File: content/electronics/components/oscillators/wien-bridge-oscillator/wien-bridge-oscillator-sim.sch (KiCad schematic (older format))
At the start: 12 parts, among them U1 AD8051

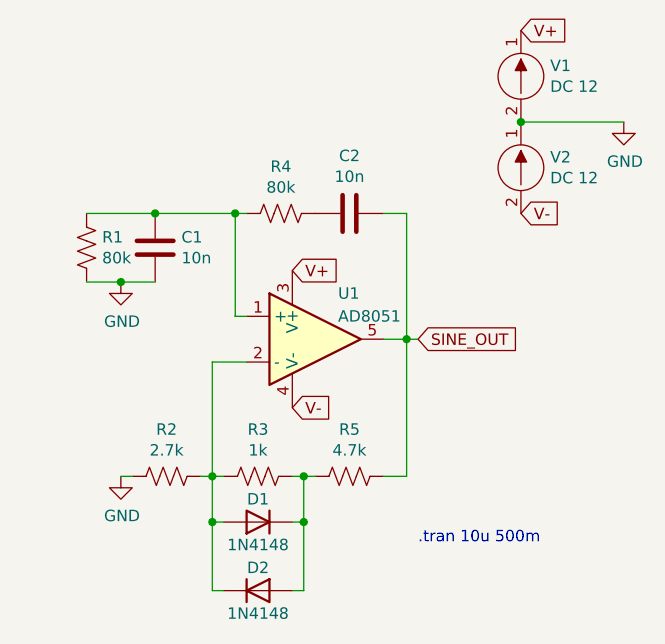
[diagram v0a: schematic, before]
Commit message: Added traditional schematics of a Wien bridge oscillator circuit.
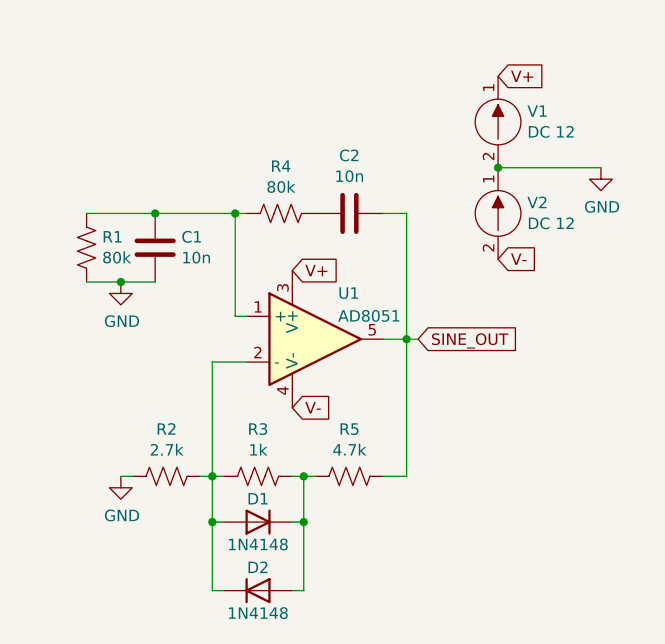
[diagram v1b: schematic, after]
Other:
- note removed: ".tran 10u 500m"
- moved on the sheet: V1, V2
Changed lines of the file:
@@
 L Bio-Sim:DC12 V1
 U 1 1 608A8BB9
-P 6200 1900
-F 0 "V1" H 6328 1946 50  0000 L CNN
-F 1 "DC 12" H 6328 1855 50  0000 L CNN
-F 2 "" H 6200 1900 50  0000 C CNN
-F 3 "" H 6200 1900 50  0000 C CNN
-F 4 "V" H 6450 1650 60  0001 C CNN "Spice_Primitive"
-F 5 "1 2" H 6450 1750 60  0001 C CNN "Spice_Node_Sequence"
-F 6 "ASK" H 6400 500 50  0001 C CNN "Substitution Category"
-	1    6200 1900
+P 6100 2100
+F 0 "V1" H 6228 2146 50  0000 L CNN
+F 1 "DC 12" H 6228 2055 50  0000 L CNN
+F 2 "" H 6100 2100 50  0000 C CNN
+F 3 "" H 6100 2100 50  0000 C CNN
+F 4 "V" H 6350 1850 60  0001 C CNN "Spice_Primitive"
+F 5 "1 2" H 6350 1950 60  0001 C CNN "Spice_Node_Sequence"
+F 6 "ASK" H 6300 700 50  0001 C CNN "Substitution Category"
+	1    6100 2100
 	1    0    0    -1
 $EndComp
@@
 L Bio-Sim:DC12 V2
 U 1 1 608A97CE
-P 6200 2300
-F 0 "V2" H 6328 2346 50  0000 L CNN
-F 1 "DC 12" H 6328 2255 50  0000 L CNN
-F 2 "" H 6200 2300 50  0000 C CNN
-F 3 "" H 6200 2300 50  0000 C CNN
-F 4 "V" H 6450 2050 60  0001 C CNN "Spice_Primitive"
-F 5 "1 2" H 6450 2150 60  0001 C CNN "Spice_Node_Sequence"
-F 6 "ASK" H 6400 900 50  0001 C CNN "Substitution Category"
-	1    6200 2300
+P 6100 2500
+F 0 "V2" H 6228 2546 50  0000 L CNN
+F 1 "DC 12" H 6228 2455 50  0000 L CNN
+F 2 "" H 6100 2500 50  0000 C CNN
+F 3 "" H 6100 2500 50  0000 C CNN
+F 4 "V" H 6350 2250 60  0001 C CNN "Spice_Primitive"
+F 5 "1 2" H 6350 2350 60  0001 C CNN "Spice_Node_Sequence"
+F 6 "ASK" H 6300 1100 50  0001 C CNN "Substitution Category"
+	1    6100 2500
 	1    0    0    -1
 $EndComp
@@
 L power:GND #PWR03
 U 1 1 608AA1F3
-P 6650 2100
-F 0 "#PWR03" H 6650 1850 50  0001 C CNN
-F 1 "GND" H 6655 1927 50  0000 C CNN
-F 2 "" H 6650 2100 50  0001 C CNN
-F 3 "" H 6650 2100 50  0001 C CNN
-	1    6650 2100
-	1    0    0    -1
-$EndComp
-Wire Wire Line
-	6650 2100 6200 2100
-Connection ~ 6200 2100
-Text GLabel 6200 2500 2    50   Input ~ 0
+P 6550 2300
+F 0 "#PWR03" H 6550 2050 50  0001 C CNN
+F 1 "GND" H 6555 2127 50  0000 C CNN
+F 2 "" H 6550 2300 50  0001 C CNN
+F 3 "" H 6550 2300 50  0001 C CNN
+	1    6550 2300
+	1    0    0    -1
+$EndComp
+Wire Wire Line
+	6550 2300 6100 2300
+Connection ~ 6100 2300
+Text GLabel 6100 2700 2    50   Input ~ 0
 V-
-Text GLabel 6200 1700 2    50   Input ~ 0
+Text GLabel 6100 1900 2    50   Input ~ 0
 V+
 Text GLabel 5200 2750 2    50   Input ~ 0
@@
 Wire Wire Line
 	4850 3150 5000 3150
-Text Notes 5750 3950 0    50   ~ 0
-.tran 10u 500m
 $EndSCHEMATC

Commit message: Updated the Wien bridge oscillator worked example.
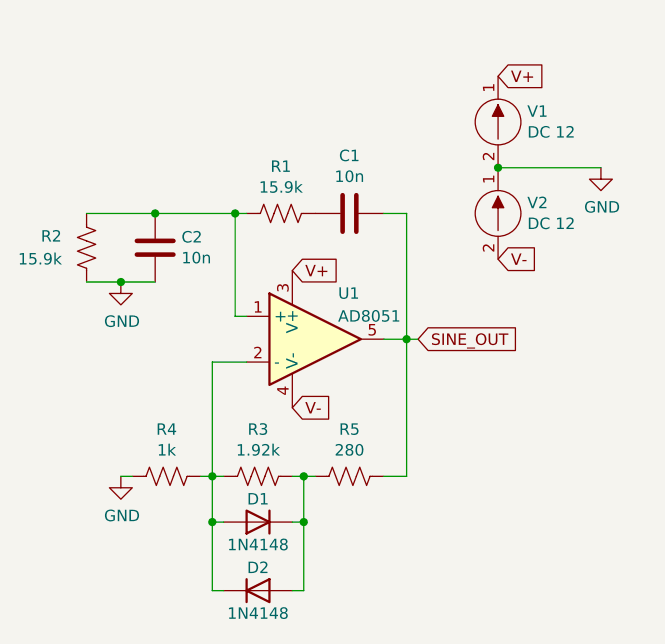
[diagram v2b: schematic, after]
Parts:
- D1, D2: Spice_Lib_File sim\\1N4148.lib -> 1N4148.lib
- R1: renamed from R4; value 80k -> 15.9k
- R2: renamed from R1; value 80k -> 15.9k
- R3: value 1k -> 1.92k
- R4: renamed from R2; value 2.7k -> 1k
- R5: value 4.7k -> 280
- U1: Spice_Lib_File sim\\AD8051.lib -> AD8051.lib
- renumbered C2 to C1, C1 to C2
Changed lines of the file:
@@
 $EndDescr
-$Comp
-L mbedded-ninja-kicad-symbols-sim:1N4148 D2
-U 1 1 608A7C60
-P 5050 4150
-F 0 "D2" H 5050 4250 50  0000 C CNN
-F 1 "1N4148" H 5050 4050 50  0000 C CNN
-F 2 "" H 5050 4150 50  0001 C CNN
-F 3 "~" H 5050 4150 50  0001 C CNN
-F 4 "D" H 5050 3650 50  0001 C CNN "Spice_Primitive"
-F 5 "1N4148" H 5050 3750 50  0001 C CNN "Spice_Model"
-F 6 "Y" H 5050 3850 50  0001 C CNN "Spice_Netlist_Enabled"
-F 7 "2 1" H 5050 3950 50  0001 C CNN "Spice_Node_Sequence"
-F 8 "sim\\1N4148.lib" H 5050 3550 50  0001 C CNN "Spice_Lib_File"
-	1    5050 4150
-	1    0    0    -1
-$EndComp
 $Comp
 L mbedded-ninja-kicad-symbols-sim:1N4148 D1
@@
 F 6 "Y" H 5050 3550 50  0001 C CNN "Spice_Netlist_Enabled"
 F 7 "2 1" H 5050 3650 50  0001 C CNN "Spice_Node_Sequence"
-F 8 "sim\\1N4148.lib" H 5050 3250 50  0001 C CNN "Spice_Lib_File"
+F 8 "1N4148.lib" H 5050 3250 50  0001 C CNN "Spice_Lib_File"
 	1    5050 3850
 	-1   0    0    1
@@
 F 5 "AD8051" H 5300 3300 50  0001 L CNN "Spice_Model"
 F 6 "Y" H 5300 3300 50  0001 L CNN "Spice_Netlist_Enabled"
-F 7 "sim\\AD8051.lib" H 5300 3300 50  0001 L CNN "Spice_Lib_File"
+F 7 "AD8051.lib" H 5300 3300 50  0001 L CNN "Spice_Lib_File"
 	1    5300 3050
 	1    0    0    -1
@@
 	5600 3050 5700 3050
 $Comp
-L mbedded-ninja-kicad-symbols-sim:10k R4
+L mbedded-ninja-kicad-symbols-sim:10k R1
 U 1 1 608B013F
 P 5150 2500
-F 0 "R4" V 4945 2500 50  0000 C CNN
-F 1 "80k" V 5036 2500 50  0000 C CNN
+F 0 "R1" V 4945 2500 50  0000 C CNN
+F 1 "15.9k" V 5036 2500 50  0000 C CNN
 F 2 "" H 5250 1800 50  0001 L CNN
 F 3 "" H 5150 2500 50  0001 L CNN
@@
 $EndComp
 $Comp
-L mbedded-ninja-kicad-symbols-sim:100n C2
+L mbedded-ninja-kicad-symbols-sim:100n C1
 U 1 1 608B0C13
 P 5450 2500
-F 0 "C2" V 5198 2500 50  0000 C CNN
+F 0 "C1" V 5198 2500 50  0000 C CNN
 F 1 "10n" V 5289 2500 50  0000 C CNN
 F 2 "" H 5650 1700 50  0001 L CNN
@@
 	5700 3050 5750 3050
 $Comp
-L mbedded-ninja-kicad-symbols-sim:10k R1
+L mbedded-ninja-kicad-symbols-sim:10k R2
 U 1 1 608B4708
 P 4300 2650
-F 0 "R1" H 4232 2604 50  0000 R CNN
-F 1 "80k" H 4232 2695 50  0000 R CNN
+F 0 "R2" H 4500 2600 50  0000 R CNN
+F 1 "15.9k" H 4600 2700 50  0000 R CNN
 F 2 "" H 4400 1950 50  0001 L CNN
 F 3 "" H 4300 2650 50  0001 L CNN
@@
 $EndComp
 $Comp
-L mbedded-ninja-kicad-symbols-sim:100n C1
+L mbedded-ninja-kicad-symbols-sim:100n C2
 U 1 1 608B5320
 P 4600 2650
-F 0 "C1" H 4485 2604 50  0000 R CNN
+F 0 "C2" H 4485 2604 50  0000 R CNN
 F 1 "10n" H 4485 2695 50  0000 R CNN
 F 2 "" H 4800 1850 50  0001 L CNN
@@
 P 5450 3650
 F 0 "R5" V 5245 3650 50  0000 C CNN
-F 1 "4.7k" V 5336 3650 50  0000 C CNN
+F 1 "280" V 5336 3650 50  0000 C CNN
 F 2 "" H 5550 2950 50  0001 L CNN
 F 3 "" H 5450 3650 50  0001 L CNN
@@
 P 5050 3650
 F 0 "R3" V 4845 3650 50  0000 C CNN
-F 1 "1k" V 4936 3650 50  0000 C CNN
+F 1 "1.92k" V 4936 3650 50  0000 C CNN
 F 2 "" H 5150 2950 50  0001 L CNN
 F 3 "" H 5050 3650 50  0001 L CNN
@@
 Wire Wire Line
 	5700 3650 5700 3050
-$Comp
-L mbedded-ninja-kicad-symbols-sim:10k R2
-U 1 1 608BF7F2
-P 4650 3650
-F 0 "R2" V 4445 3650 50  0000 C CNN
-F 1 "2.7k" V 4536 3650 50  0000 C CNN
-F 2 "" H 4750 2950 50  0001 L CNN
-F 3 "" H 4650 3650 50  0001 L CNN
-F 4 "R" H 4800 3500 50  0001 C CNN "Spice_Primitive"
-	1    4650 3650
-	0    1    1    0
-$EndComp
 $Comp
 L power:GND #PWR02
@@
 Wire Wire Line
 	4850 3150 5000 3150
+$Comp
+L mbedded-ninja-kicad-symbols-sim:10k R4
+U 1 1 608BF7F2
+P 4650 3650
+F 0 "R4" V 4445 3650 50  0000 C CNN
+F 1 "1k" V 4536 3650 50  0000 C CNN
+F 2 "" H 4750 2950 50  0001 L CNN
+F 3 "" H 4650 3650 50  0001 L CNN
+F 4 "R" H 4800 3500 50  0001 C CNN "Spice_Primitive"
+	1    4650 3650
+	0    1    1    0
+$EndComp
+$Comp
+L mbedded-ninja-kicad-symbols-sim:1N4148 D2
+U 1 1 608A7C60
+P 5050 4150
+F 0 "D2" H 5050 4250 50  0000 C CNN
+F 1 "1N4148" H 5050 4050 50  0000 C CNN
+F 2 "" H 5050 4150 50  0001 C CNN
+F 3 "~" H 5050 4150 50  0001 C CNN
+F 4 "D" H 5050 3650 50  0001 C CNN "Spice_Primitive"
+F 5 "1N4148" H 5050 3750 50  0001 C CNN "Spice_Model"
+F 6 "Y" H 5050 3850 50  0001 C CNN "Spice_Netlist_Enabled"
+F 7 "2 1" H 5050 3950 50  0001 C CNN "Spice_Node_Sequence"
+F 8 "1N4148.lib" H 5050 3550 50  0001 C CNN "Spice_Lib_File"
+	1    5050 4150
+	1    0    0    -1
+$EndComp
 $EndSCHEMATC
